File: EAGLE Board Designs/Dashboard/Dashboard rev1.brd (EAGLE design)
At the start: 160 x 101.5 mm, 45 parts, among them IC1 LM340S, U1 ATMEGA328P-AU, X2 CONNECTOR-6NANO-FIT_VERTICAL-6, X3 CONNECTOR-8NANO-FIT_VERTICAL-8

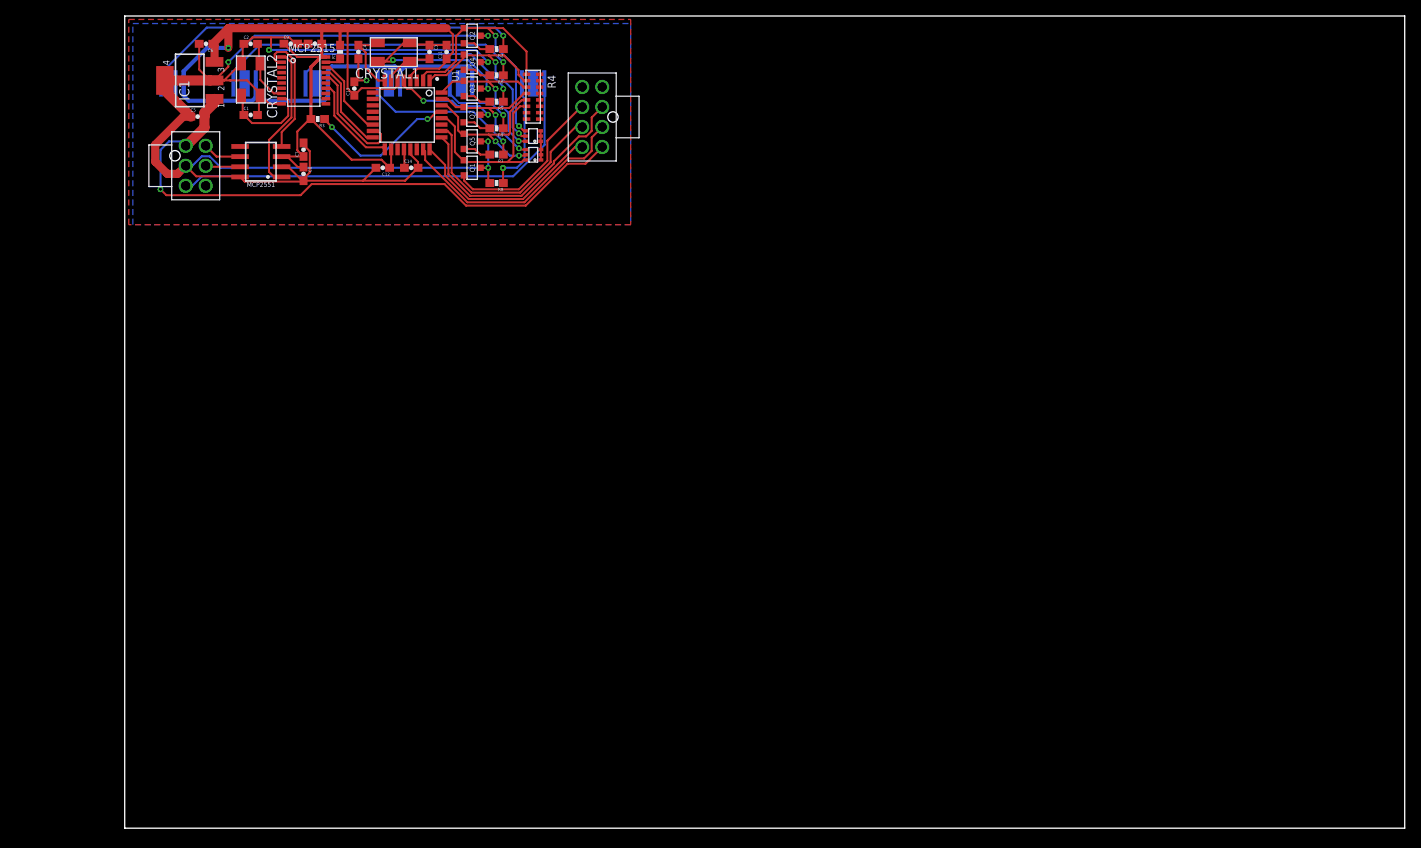
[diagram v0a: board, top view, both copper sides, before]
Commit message: added outline and holes
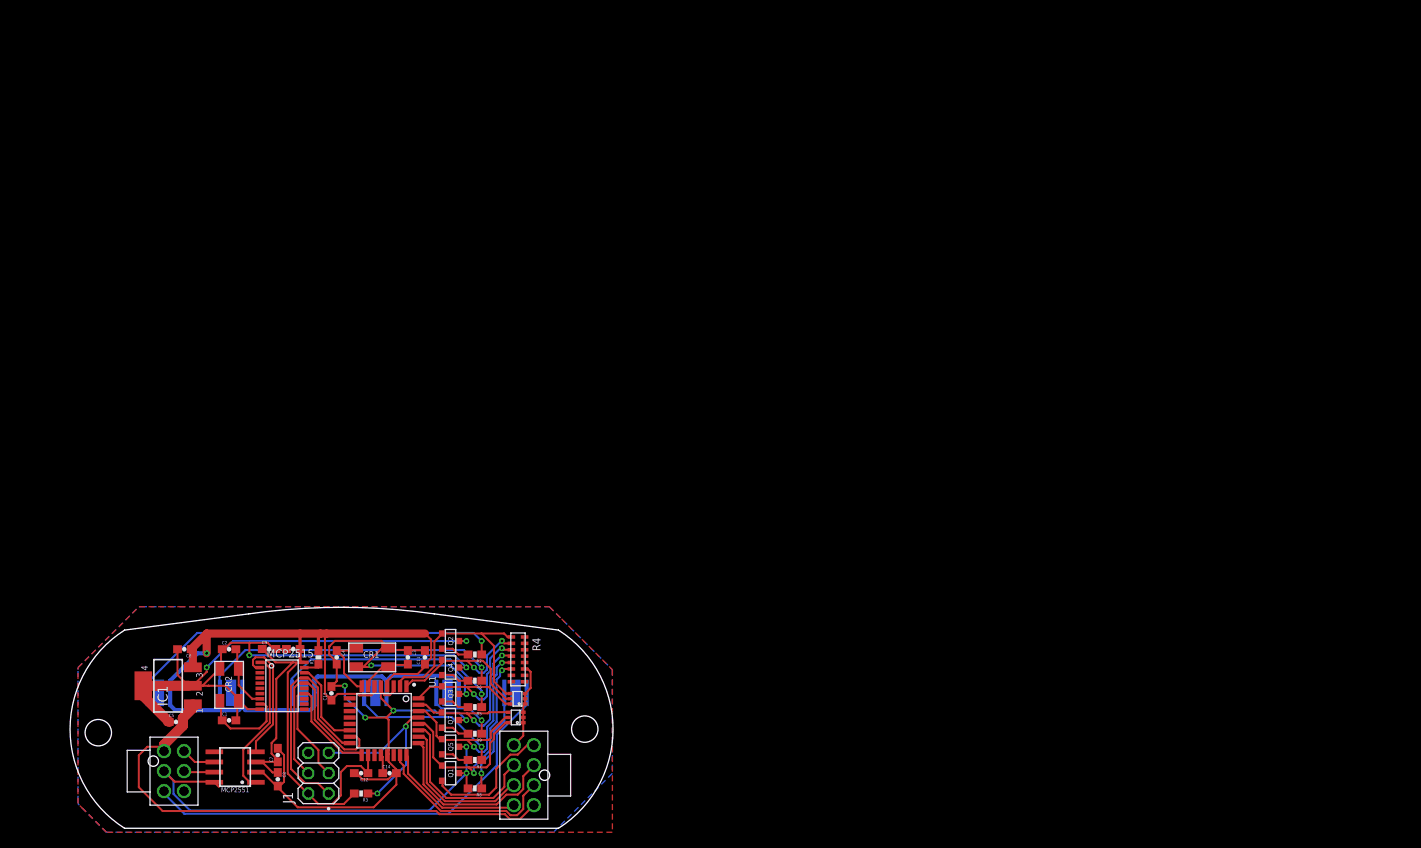
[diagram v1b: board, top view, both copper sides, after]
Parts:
- removed CRYSTAL1, CRYSTAL2: 16MHz, 10pF, HyTechDevices:ABM3B
- added CR1, CR2: 16MHz, 10pF, HyTechDevices:ABM3B
- added J1: AVR-ISP-HEADER, HyTechDevices:2X03
- moved R3 84.5 mm to (29.5, 4.34)
- moved X3 82.7 mm to (51.1, 6.63)
- moved SSOK 76.2 mm to (50.5, 15.3)
- moved AMS_FAULT 76.2 mm to (33.0, 15.3)
- moved IMD_FAULT 76.2 mm to (42.0, 15.3)
- moved MC_ERR 76.2 mm to (14.9, 15.3)
- moved MODE 76.2 mm to (24.0, 15.3)
- moved START 76.2 mm to (5.93, 15.3)
- moved U1 75.8 mm to (32.4, 13.4)
- moved C7 75.7 mm to (19.1, 9.14)
- moved C8 75.7 mm to (19.1, 6.12)
- moved MCP2551 75.7 mm to (13.8, 7.64)
- moved C11 75.7 mm to (37.5, 21.4)
- moved C3 75.7 mm to (35.4, 21.4)
- moved C4 75.7 mm to (26.5, 21.4)
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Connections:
- removed net N$7: R3.1, U1.29
- new net BTN_EXTRA: U1.27, X3.P$7
- new net RESET: J1.5, R3.1, U1.29
- net +5V: now also J1.2
- net BUZZER_OUT: now also X3.P$4; no longer X3.P$7
- net GND: now also CR1.P$2, CR1.P$4, CR2.P$2, CR2.P$4, J1.6; no longer CRYSTAL1.P$2, CRYSTAL1.P$4, CRYSTAL2.P$2, CRYSTAL2.P$4
- net MISO: now also J1.1
- net MOSI: now also J1.4
- net N$2: now also CR2.P$3; no longer CRYSTAL2.P$3
- net N$3: now also CR2.P$1; no longer CRYSTAL2.P$1
- net N$5: now also CR1.P$1; no longer CRYSTAL1.P$1
- net N$6: now also CR1.P$3; no longer CRYSTAL1.P$3
- net SCK: now also J1.3
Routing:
- net GND: track 270.2 -> 295.9 mm, vias 11 -> 12
- net RESET: track 0.00 -> 24.3 mm, vias 0 -> 2
- net BTN_EXTRA: track 0.00 -> 21.5 mm
- net N$7: track 18.8 -> 0.00 mm, vias 2 -> 0
- net MISO: track 11.3 -> 29.7 mm
- net MOSI: track 14.5 -> 27.8 mm
- net BUZZER_CTRL: track 23.3 -> 36.2 mm, vias 0 -> 2
- net SCK: track 12.2 -> 24.4 mm
- net +5V: track 172.2 -> 184.1 mm
- net +12V: track 76.4 -> 66.9 mm, vias 1 -> 0
- net LED_AMS_CTRL: track 22.3 -> 31.4 mm
- net LED_START_CTRL: track 36.8 -> 28.3 mm, vias 2 -> 0
- net BTN_START_READ: track 27.7 -> 19.3 mm
- net BTN_MC_CYCLE_READ: track 31.0 -> 23.3 mm
- net BTN_MODE_READ: track 25.1 -> 17.5 mm
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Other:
- board size 160 x 101.5 mm -> 67.9 x 27.6 mm

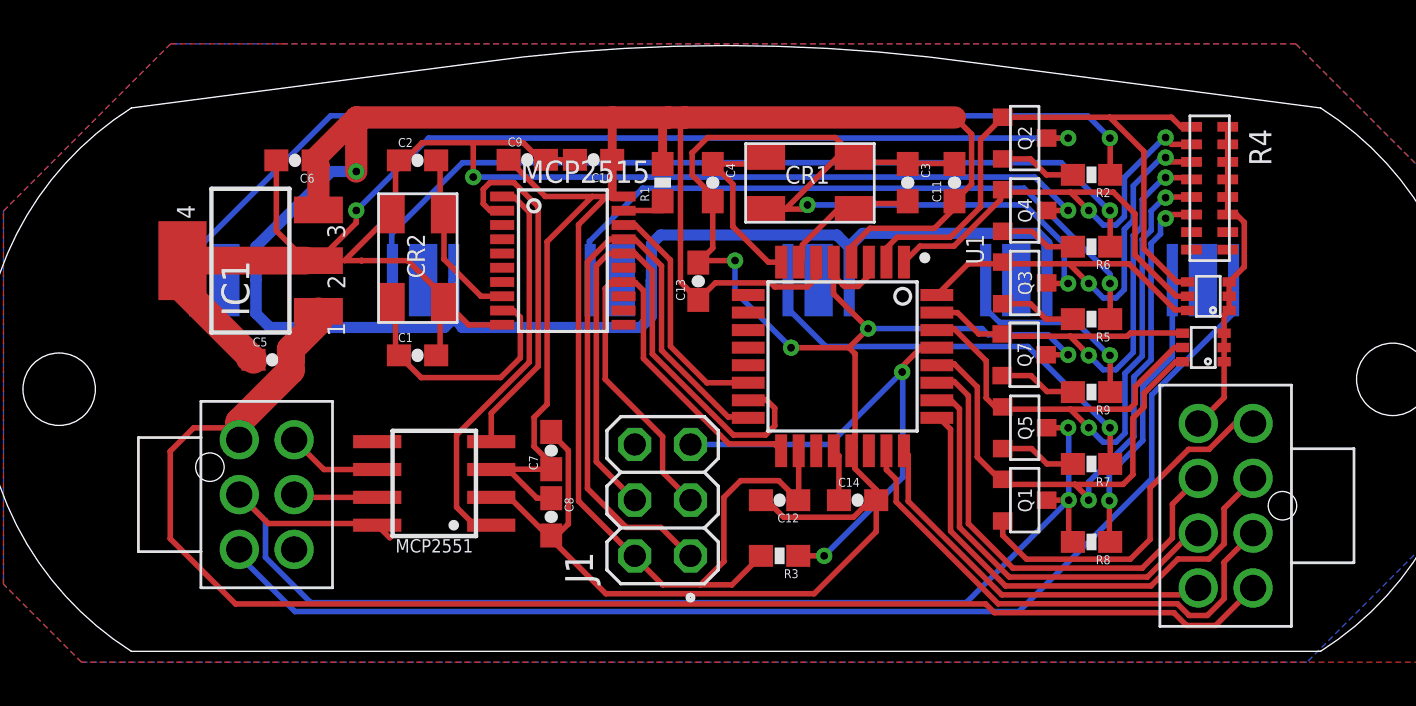
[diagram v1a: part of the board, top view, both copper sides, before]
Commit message: layout done, still need to finish silkscreen
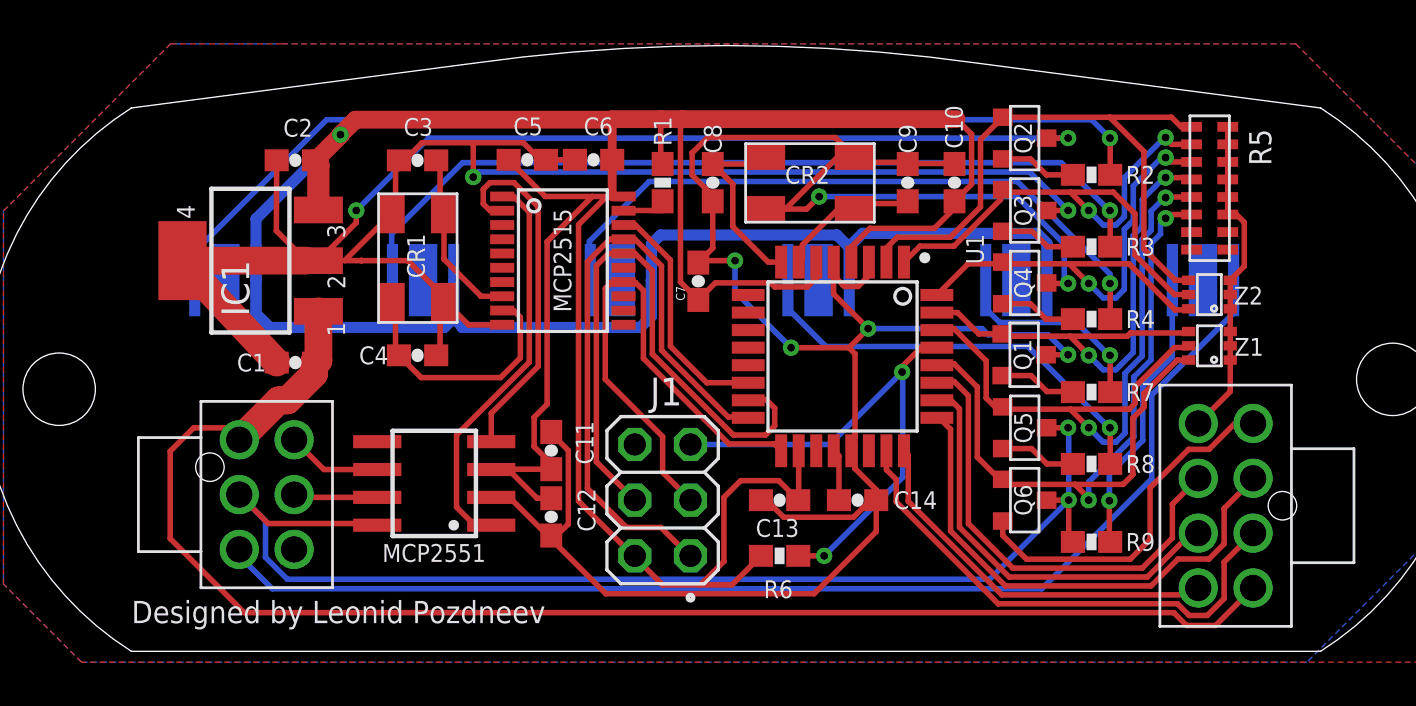
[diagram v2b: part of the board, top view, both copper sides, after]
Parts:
- removed Q7: (no value), HyTechDevices:SOT23
- removed U$2, U$3: MMBZ5245BTS-7-F, HyTechDevices:SOT363
- added Q6: (no value), HyTechDevices:SOT23
- added Z1, Z2: MMBZ5245BTS-7-F, HyTechDevices:SOT363
- C1: value 14pF -> 0.22uF
- C11: value 0.1uF -> 1uF
- C2: value 14pF -> 0.1uF
- C5: value 0.22uF -> 1uF
- C7: value 1uF -> 0.1uF
- C8: value 0.1uF -> 14pF
- C9: value 1uF -> 14pF
- R3: value 10k -> (none)
- R4: value 10k -> (none); device HyTechDevices:CAT16-*8 -> HyTechDevices:0603-RES
- R5: value (none) -> 10k; device HyTechDevices:0603-RES -> HyTechDevices:CAT16-*8
- R6: value (none) -> 10k
- moved CR1 22.7 mm to (11.3, 20.8), turned to 270 degrees
- moved CR2 22.7 mm to (33.9, 23.1), turned to 180 degrees
- moved C3 22.4 mm to (13.0, 22.4), turned to 0 degrees
- moved C11 22.1 mm to (19.1, 9.14)
- moved R3 20.0 mm to (43.8, 18.4)
- moved R6 20.0 mm to (29.5, 4.34)
- moved C9 17.4 mm to (35.4, 21.4), turned to 270 degrees
- moved C8 16.9 mm to (26.5, 21.4)
- moved C10 16.5 mm to (37.5, 21.4), turned to 90 degrees
- moved C4 15.6 mm to (13.0, 13.5), turned to 0 degrees
- moved C5 14.8 mm to (18.0, 22.4)
- moved C6 13.6 mm to (21.1, 22.4)
- moved C13 10.6 mm to (29.5, 6.88), turned to 180 degrees
- moved C12 10.4 mm to (19.1, 6.12), turned to 270 degrees
- moved C7 10.2 mm to (25.8, 16.9)
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- renumbered AMS_FAULT to AMS, IMD_FAULT to IMD, MC_ERR to MC, X2 to X1, X3 to $$X2
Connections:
- net +12V: now also C1.2; no longer C5.2
- net +5V: now also C2.1, C5.1, R6.2; no longer C8.1, C9.1, R3.2
- net BUZZER_CTRL: now also Q6.1, R5.P$6, Z1.P$4; no longer Q1.1, R4.P$6, U$3.P$4
- net BUZZER_OUT: now also Q6.2; no longer Q1.2
- net GND: now also C1.1, C2.2, C5.2, C9.1, Q6.3, R5.P$11, R5.P$12, R5.P$13, R5.P$14, R5.P$15, R5.P$16, R9.2, Z1.P$1, Z1.P$2, Z1.P$3, Z2.P$1, Z2.P$2, Z2.P$3; no longer C1.2, C2.1, C5.1, C9.2, Q7.3, R4.P$11, R4.P$12, R4.P$13, R4.P$14, R4.P$15, R4.P$16, R8.2, U$2.P$1, U$2.P$2, U$2.P$3, U$3.P$1, U$3.P$2, U$3.P$3
- net LED_AMS_CTRL: now also R5.P$5, Z1.P$5; no longer R4.P$5, U$3.P$5
- net LED_IMD_CTRL: now also Q1.1, R5.P$4, Z1.P$6; no longer Q7.1, R4.P$4, U$3.P$6
- net LED_MC_ERR_CTRL: now also Q3.1, R5.P$2, Z2.P$5; no longer Q4.1, R4.P$2, U$2.P$5
- net LED_MODE_CTRL: now also Q4.1, R5.P$3, Z2.P$4; no longer Q3.1, R4.P$3, U$2.P$4
- net LED_START_CTRL: now also R5.P$1, Z2.P$6; no longer R4.P$1, U$2.P$6
- net N$10: now also R4.1; no longer R5.1
- net N$12: now also Q1.2, R7.2; no longer Q7.2, R9.2
- net N$13: now also R7.1; no longer R9.1
- net N$15: now also R9.1; no longer R8.1
- net N$16: now also R8.1; no longer R7.1
- net N$17: now also R8.2; no longer R7.2
- net N$18: now also Q3.2, R3.2; no longer Q4.2, R6.2
- net N$19: now also R3.1; no longer R6.1
- net N$2: now also C4.1, CR1.P$3; no longer C1.1, CR2.P$3
- net N$3: now also C3.2, CR1.P$1; no longer C2.2, CR2.P$1
- net N$5: now also C9.2, CR2.P$1; no longer C3.2, CR1.P$1
- net N$6: now also C8.1, CR2.P$3; no longer C4.1, CR1.P$3
- net N$9: now also Q4.2, R4.2; no longer Q3.2, R5.2
- net RESET: now also R6.1; no longer R3.1
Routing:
- net +5V: track 184.1 -> 181.9 mm
- net GND: track 295.9 -> 294.4 mm
- net SSOK: track 56.1 -> 55.2 mm
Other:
- board text added: "Designed by Leonid Pozdneev"
- board text added: "MCP2551"
- board text added: "Z1"
- board text added: "Z2"

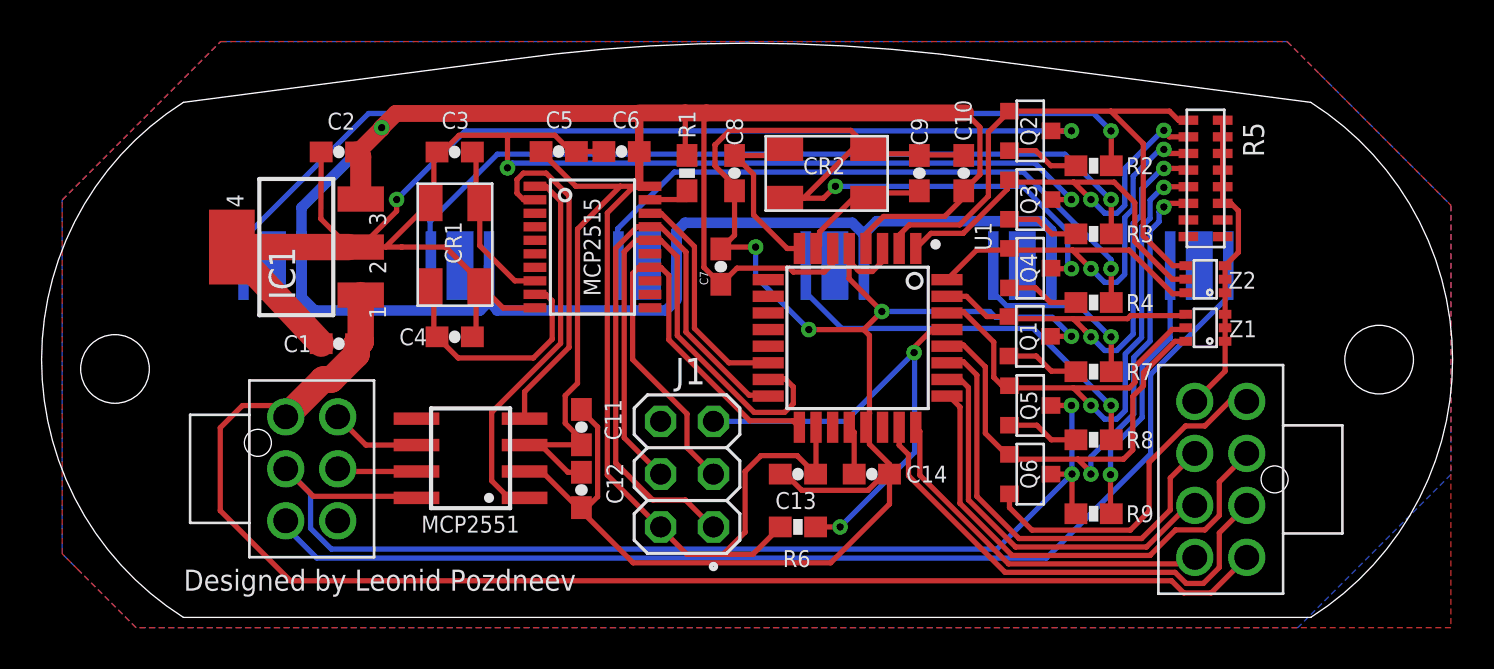
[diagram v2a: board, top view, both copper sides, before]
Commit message: done with dashboard layout, i hope
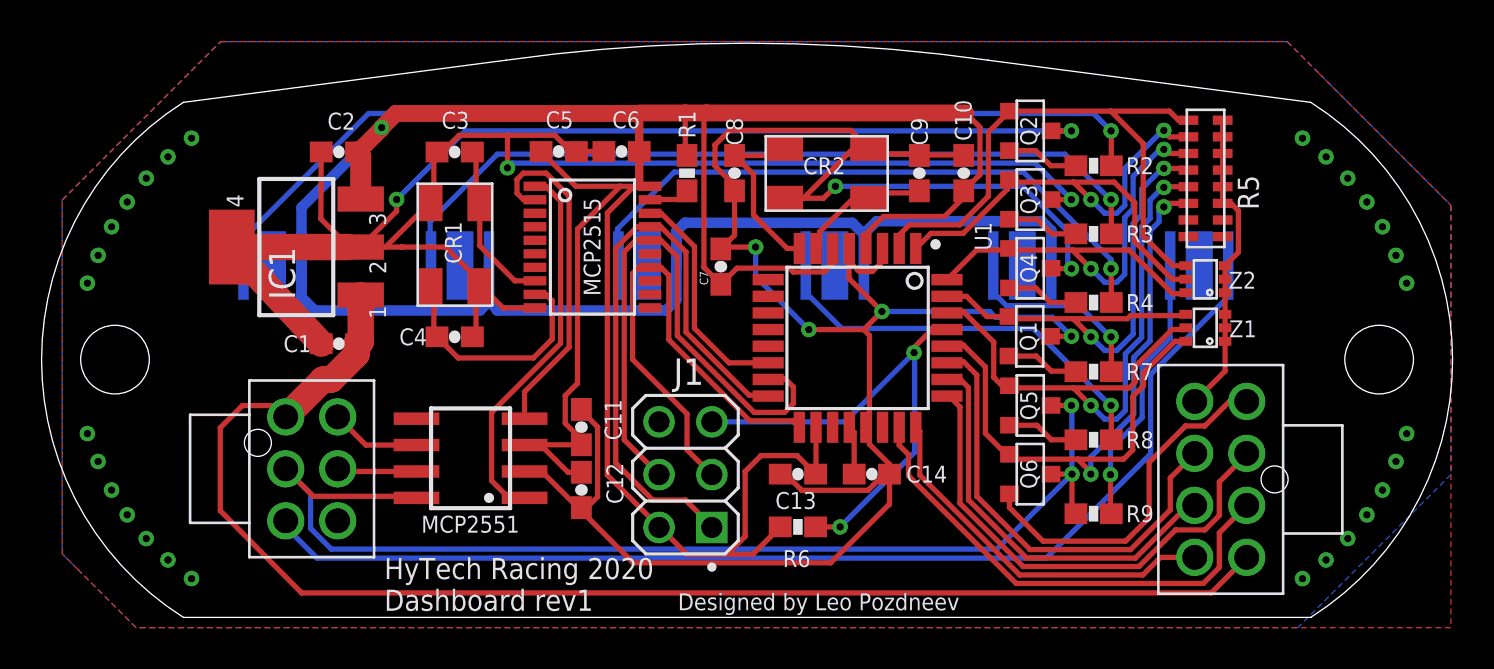
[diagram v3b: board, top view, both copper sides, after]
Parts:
- moved J1 0.08 mm to (24.1, 6.85)
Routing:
- net BUZZER_OUT: track 16.5 -> 17.1 mm
- net GND: vias 12 -> 40
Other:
- board text added: "Designed by Leo Pozdneev"
- board text added: "HyTech Racing 2020 Dashboard rev1"
- board text removed: "Designed by Leonid Pozdneev"
